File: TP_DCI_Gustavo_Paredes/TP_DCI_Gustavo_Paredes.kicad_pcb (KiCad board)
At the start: 2 copper layers, 50 x 67 mm, 32 parts, among them J101 Conector, J102 DB9 Hembra, J103 DB9 Macho, J104 Conector +5V, U101 LTC1485, U102 LTC1485

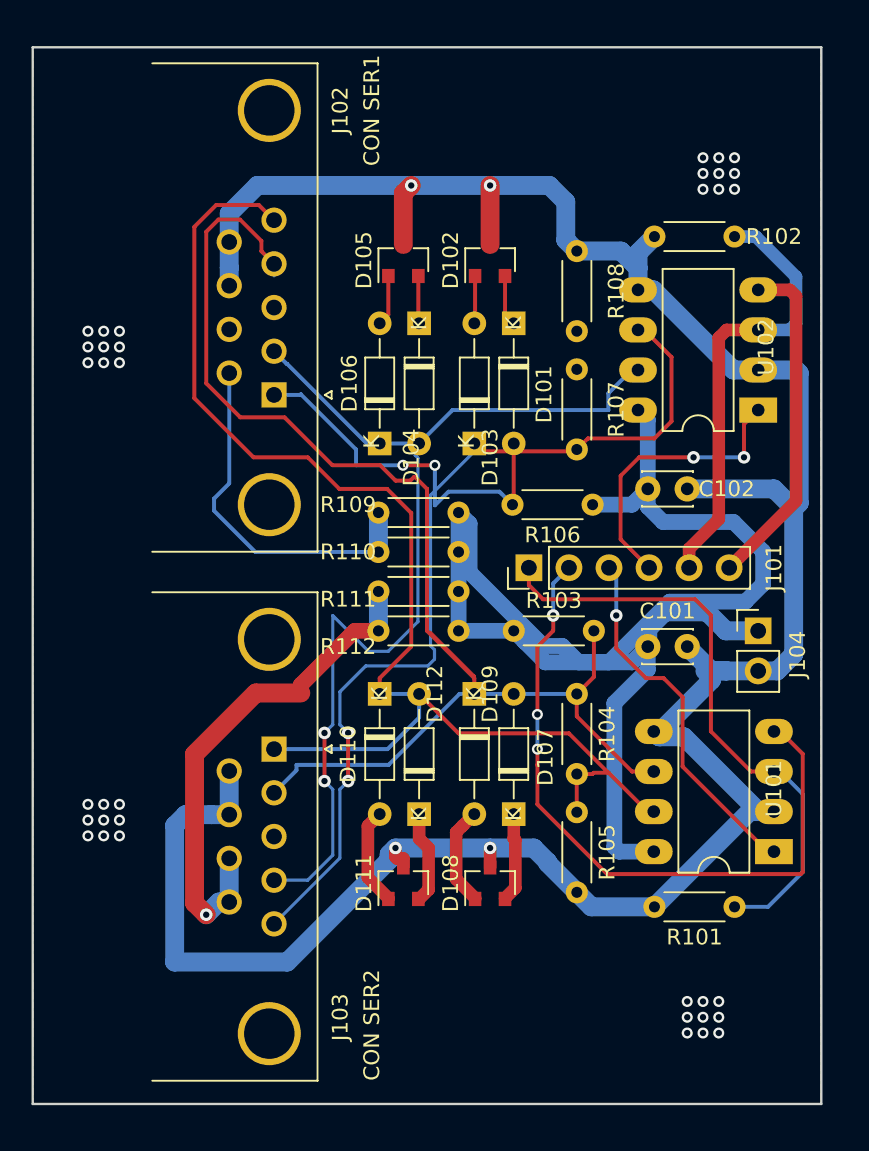
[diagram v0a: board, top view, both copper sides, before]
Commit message: PCB V4
Se aplicarons las correciones del Docente.
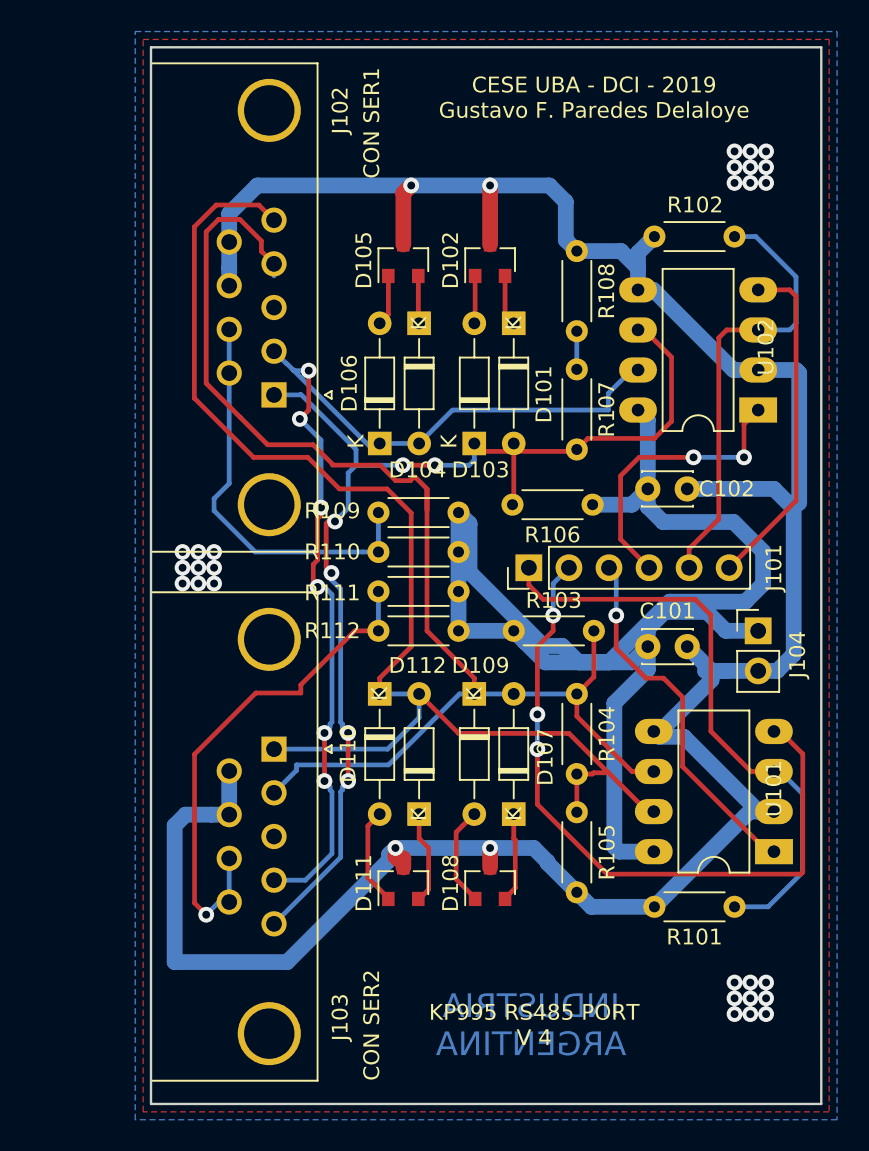
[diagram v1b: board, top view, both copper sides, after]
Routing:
- net /B_Data_N: track 82.6 -> 72.6 mm, vias 4 -> 6
- net /A_Data_N: track 88.4 -> 83.3 mm
- net Net-(J102-Pad6): track 23.1 -> 25.9 mm
- net Net-(R107-Pad2): track 0.00 -> 2.42 mm
- net GNDD: track 171.9 -> 171.4 mm, vias 40 -> 31
- net /B_Data_P: vias 2 -> 6
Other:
- board size 50 x 67 mm -> 42.5 x 67 mm
- net class Data added: clearance 0.5, trace_width 0.3, via_dia 1, via_drill 0.5
- net class Default: trace_width 0.25 -> 0.3; via_dia 0.7 -> 1; via_drill 0.4 -> 0.5
- net class Line added: clearance 0.5, trace_width 0.3, via_dia 1, via_drill 0.5
- net class Nets Tipo 1 added: clearance 0.5, trace_width 0.3, via_dia 1, via_drill 0.5
- net class Power added: clearance 0.5, trace_width 1, via_dia 1, via_drill 0.5
- rule trace_min: 0.2 -> 0.3
- rule via_min_size: 0.4 -> 0.7
- board text added: "CESE UBA - DCI - 2019 Gustavo F. Paredes Delaloye"
- board text added: "Capas de Cu = 2 Grilla = 0,5 mm Anchos de pista = 0,25/0,8/1 mm Via (min) = 0,7 mm Agujero de via (min) = 0,4 mm"
- board text added: "Estándares de fabricación de Mayer 6 MILS Diámetro de agujero 16 (0,40 mm) Diámetro de pad o vía 28 (0,70 mm) Ancho de traza 5 (0,125 mm) Separación entre trazas 5 (0,125 mm) Separación entre traza y pad/vía 5 (0,125 mm) Distancia de cobre a borde 12 (0,30 mm) Altura - trazo de letras 30 - 5"
- board text added: "KP995 RS485 PORT V 4"
- board text removed: "Ancho de pista (min) = 0,250 mm Via (min) = 0,7 mm Agujero de via (min) = 0,4 mm"
- board text removed: "CESE UBA - DCI - 7ma Cohorte Gustavo F. Paredes Delaloye"
- board text removed: "Estándares de fabricación de Mayer Diámetro de agujero 16 (0,40 mm) Diámetro de pad o vía 28 (0,70 mm) Ancho de traza 5 (0,125 mm) Separación entre trazas 5 (0,125 mm) Separación entre traza y pad/vía 5 (0,125 mm) Distancia de cobre a borde 12 (0,30 mm) Altura - trazo de letras 30 - 5"
- board text removed: "KP995 RS485 PORT"
